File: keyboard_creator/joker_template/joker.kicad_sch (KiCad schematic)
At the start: 20 parts, among them U1 BL24C256A-SFRC, U2 STM32F411CEU6, X1 ARM JTAG, Y1 7325-0800A2010-00

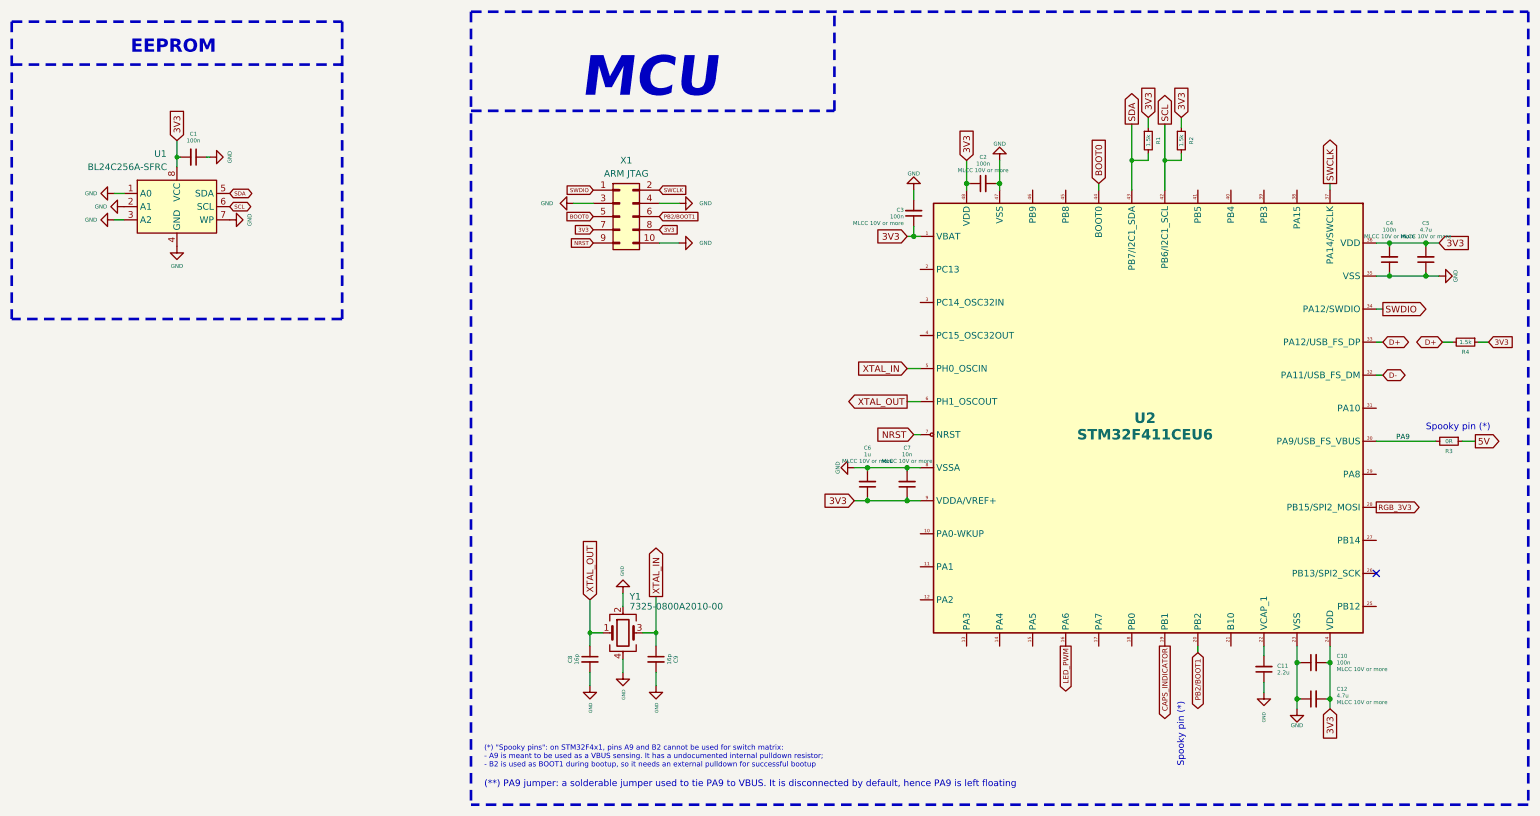
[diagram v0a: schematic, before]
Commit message: Update joker template to second revision
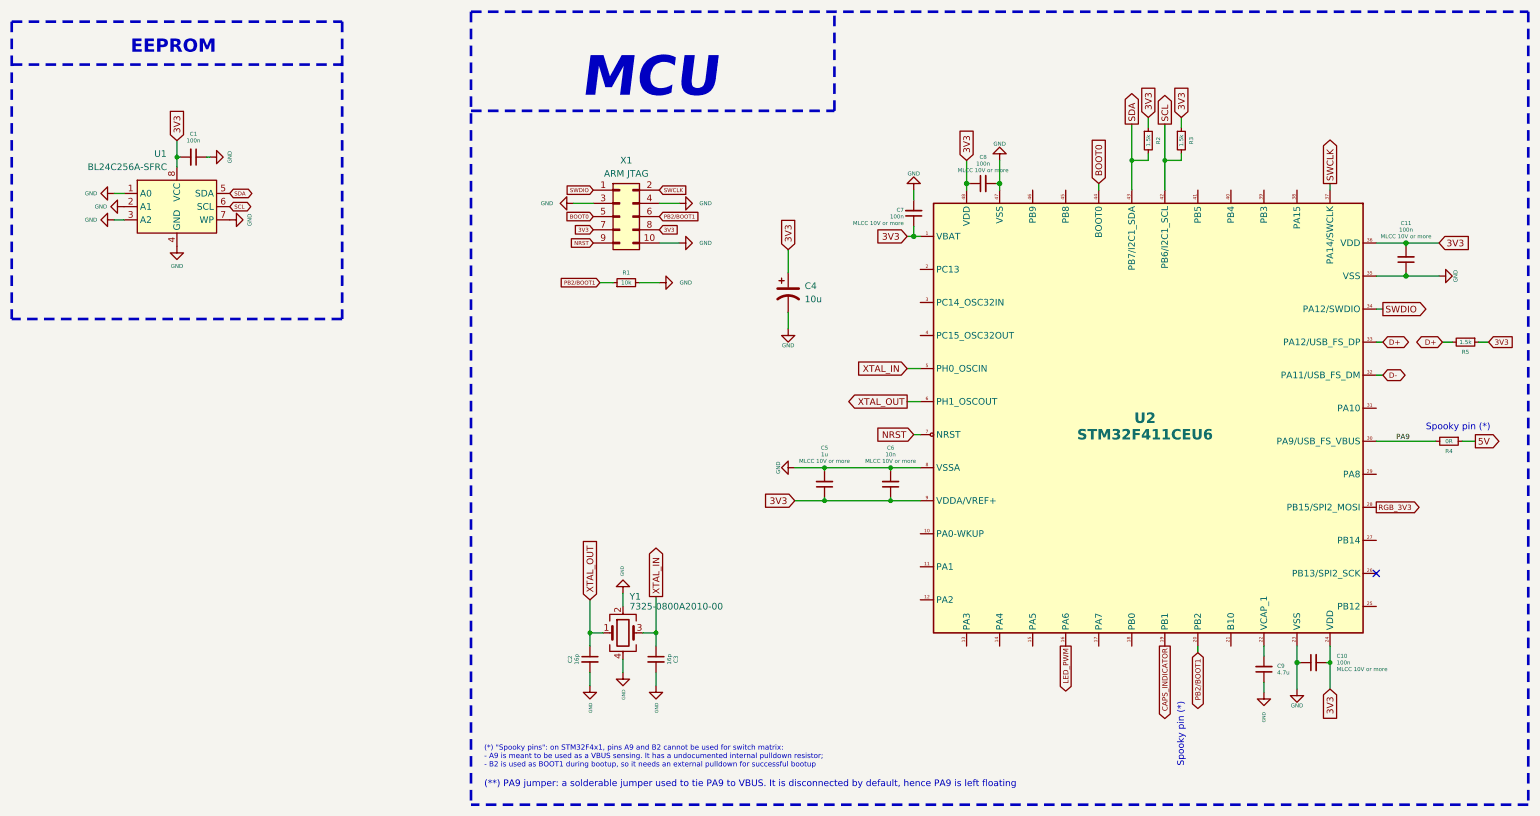
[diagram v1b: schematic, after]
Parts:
- removed C12, C5: 4.7u, Capacitor_SMD:C_0402_1005Metric, symbol Device:C_Small
- added C4: 10u, acheron_Components:CP_EIA-3216-10_Kemet-I_Pad1.58x1.35mm_HandSolder, symbol Device:CP1
- added R1: 10k, Resistor_SMD:R_0805_2012Metric, symbol Device:R_Small
- C9: renamed from C11; value 2.2u -> 4.7u
- renumbered C4 to C11, C8 to C2, C9 to C3, C6 to C5, C7 to C6, C3 to C7, C2 to C8, R1 to R2, R2 to R3, R3 to R4, R4 to R5
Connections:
- net 3V3: now also C4.1
- net GND: now also C4.2, R1.2
- net PB2/BOOT1: now also R1.1
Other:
- moved on the sheet: C11, C5, C6

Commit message: Added KiCAD Dockerfile for building kicad nightly
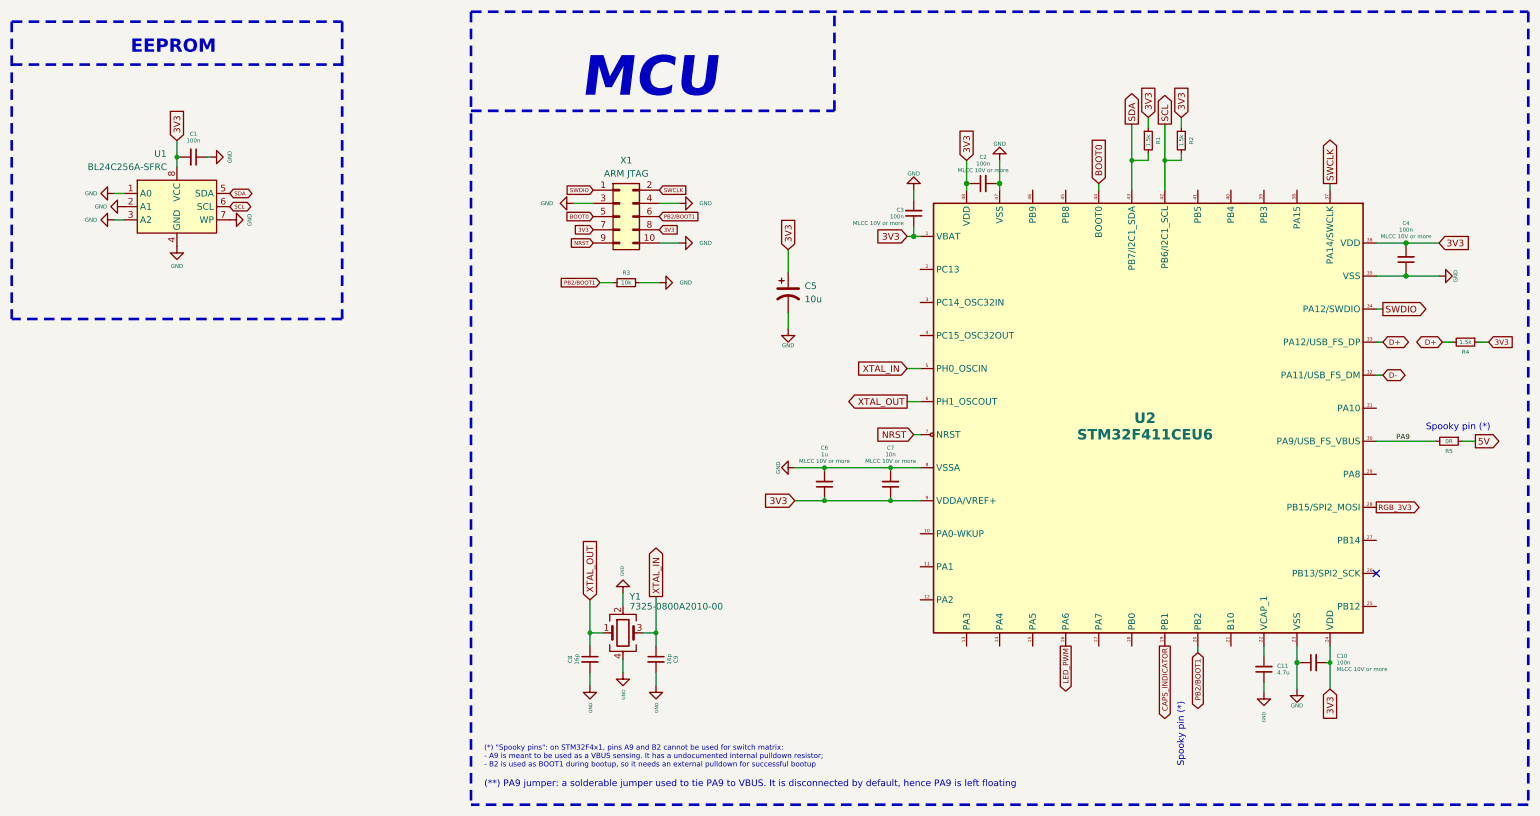
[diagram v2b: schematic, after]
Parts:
- renumbered C9 to C11, C8 to C2, C7 to C3, C11 to C4, C4 to C5, C5 to C6, C6 to C7, C2 to C8, C3 to C9, R2 to R1, R3 to R2, R1 to R3, R5 to R4, R4 to R5
